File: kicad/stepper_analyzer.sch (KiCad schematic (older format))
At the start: 32 parts, among them J1 Conn_01x04_Male, J2 Conn_01x04_Male, J3 Conn_01x40_Female, J4 Conn_02x20_Odd_Even, M1 Stepper_Motor_bipolar, U1 blackpill_STM32F401CEUx, U2 ACS70331EESATR-2P5B3, U3 ACS70331EESATR-2P5B3, U4 AT24C02D-SSHM-T

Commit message: Removed the DO NOT POPULATE comment for the 10uf caps since they are populated in the prototype.
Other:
- note removed: "Do not\npopulate"
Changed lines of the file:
@@
 Wire Wire Line
 	3850 4700 3850 4750
-Text Notes 4000 4650 0    50   ~ 0
-Do not\npopulate
-Text Notes 800  6550 0    50   ~ 0
-Do not\npopulate
 $Comp
 L Memory_EEPROM:M24C02-FMN U4

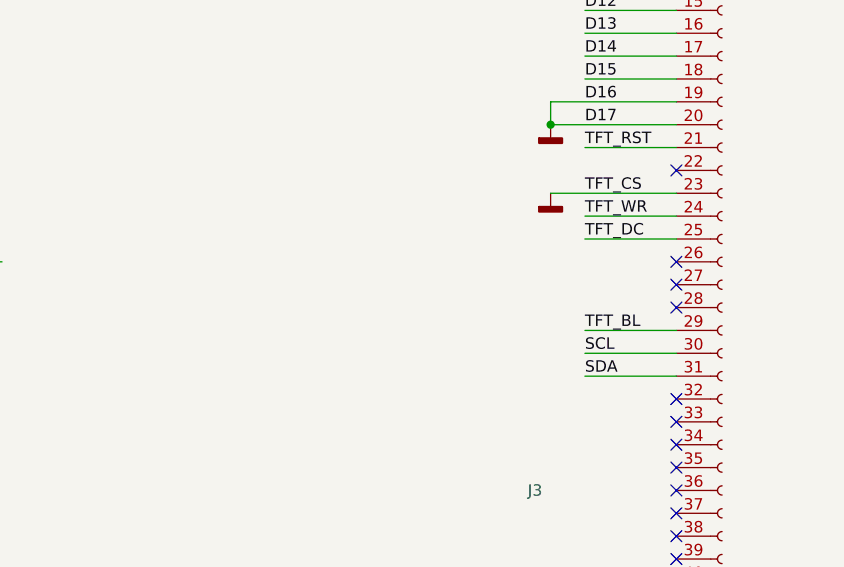
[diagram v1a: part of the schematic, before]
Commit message: Added an errata regarding floating TFT pin 26.
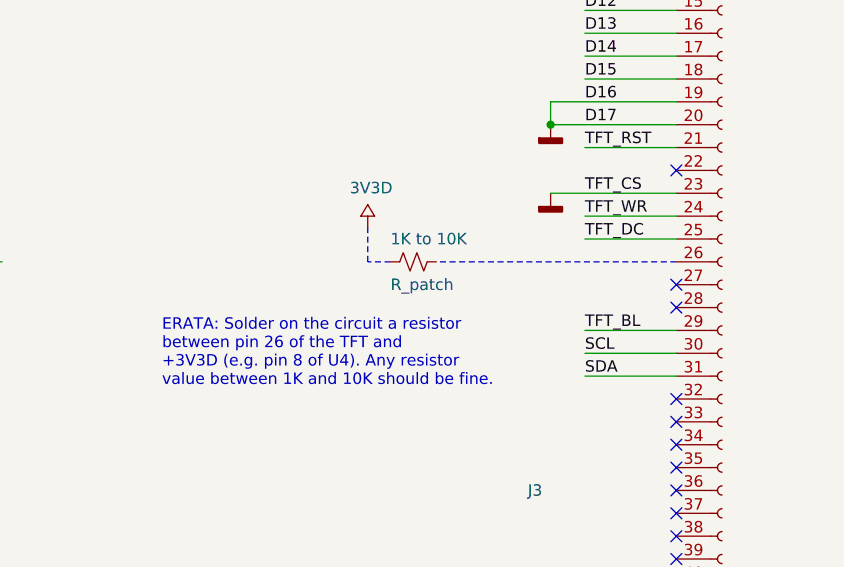
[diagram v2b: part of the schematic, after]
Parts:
- added R_patch: 1K to 10K, Resistor_SMD:R_0603_1608Metric_Pad1.05x0.95mm_HandSolder, symbol Device:R_Small_US
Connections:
- no-connect marks 31 -> 30
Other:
- note added: "ERATA: Solder on the circuit a resistor\nbetween pin 26 of the TFT and\n+3V3D (e.g. pin 8 of U4). Any resistor\nvalue between 1K and 10K should be fine."
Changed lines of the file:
@@
 TFT_RST
 NoConn ~ 6900 4050
-NoConn ~ 6900 4450
 NoConn ~ 6900 4550
 NoConn ~ 6900 5050
@@
 	0    1    1    0
 $EndComp
+$Comp
+L Device:R_Small_US R_patch
+U 1 1 60A2046F
+P 5750 4450
+F 0 "R_patch" V 5850 4350 50  0000 L CNN
+F 1 "1K to 10K" V 5650 4350 50  0000 L CNN
+F 2 "Resistor_SMD:R_0603_1608Metric_Pad1.05x0.95mm_HandSolder" H 5750 4450 50  0001 C CNN
+F 3 "~" H 5750 4450 50  0001 C CNN
+	1    5750 4450
+	0    1    1    0
+$EndComp
+Wire Notes Line
+	6900 4450 5850 4450
+Wire Notes Line
+	5650 4450 5550 4450
+Wire Notes Line
+	5550 4450 5550 4300
+Text Notes 4650 5000 0    50   ~ 0
+ERATA: Solder on the circuit a resistor\nbetween pin 26 of the TFT and\n+3V3D (e.g. pin 8 of U4). Any resistor\nvalue between 1K and 10K should be fine.
+$Comp
+L local:3V3D #PWR?
+U 1 1 60A3822B
+P 5550 4300
+F 0 "#PWR?" H 5550 4150 50  0001 C CNN
+F 1 "3V3D" H 5565 4473 50  0000 C CNN
+F 2 "" H 5550 4300 50  0001 C CNN
+F 3 "" H 5550 4300 50  0001 C CNN
+	1    5550 4300
+	1    0    0    -1
+$EndComp
 $EndSCHEMATC
